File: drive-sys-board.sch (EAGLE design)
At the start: 31 parts, among them J2 APP_2POS_CONFIG12V_HORIZ, U1 OKI-78SR-5/1.5-W36HC, U2 MAX232D, U3 MAX232D, U4 MAX232D

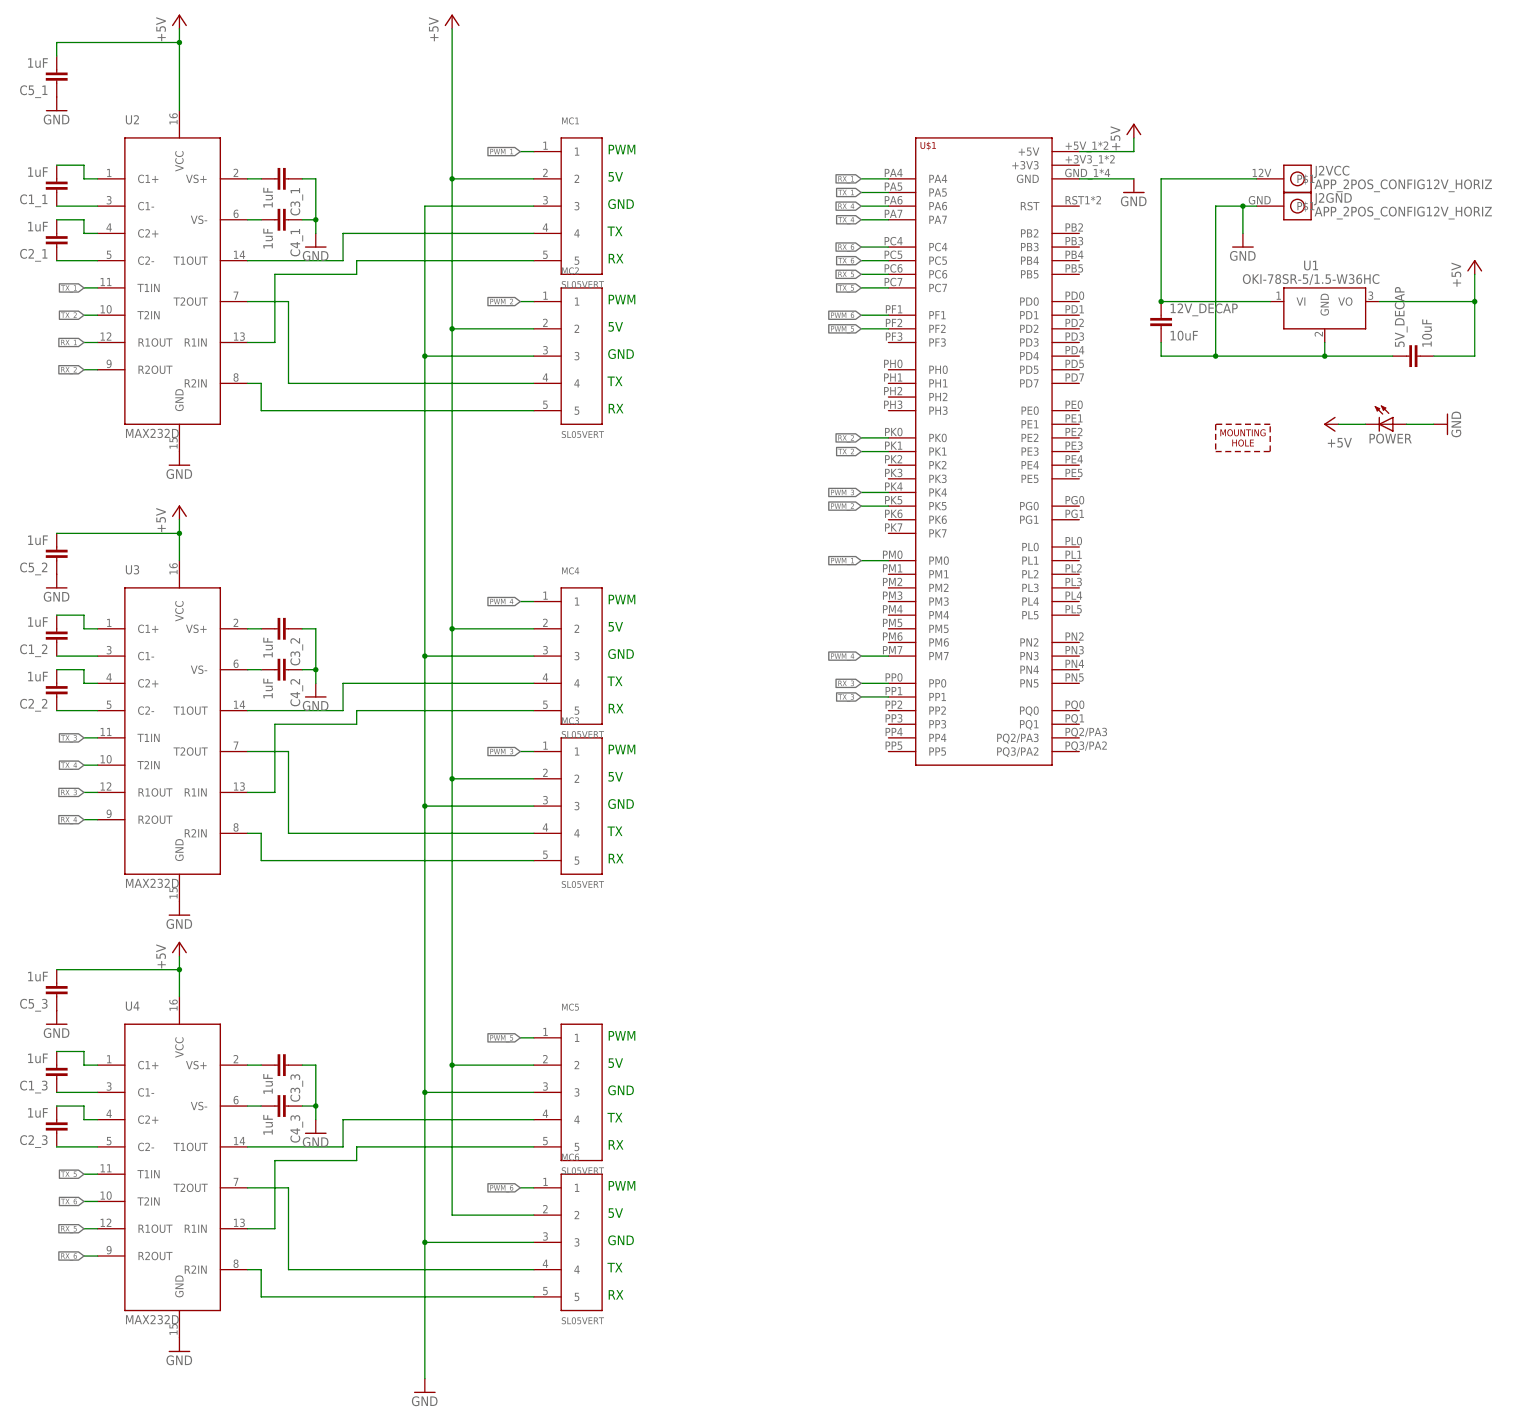
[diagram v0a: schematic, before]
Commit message: Prep for Board Review
- Labeled schematic with corresponding Serial channels (from hardware
serial on Tiva.
- Added Power Indicator LED and Debug LED
- Still need to decide on current limiting resistors for LEDs
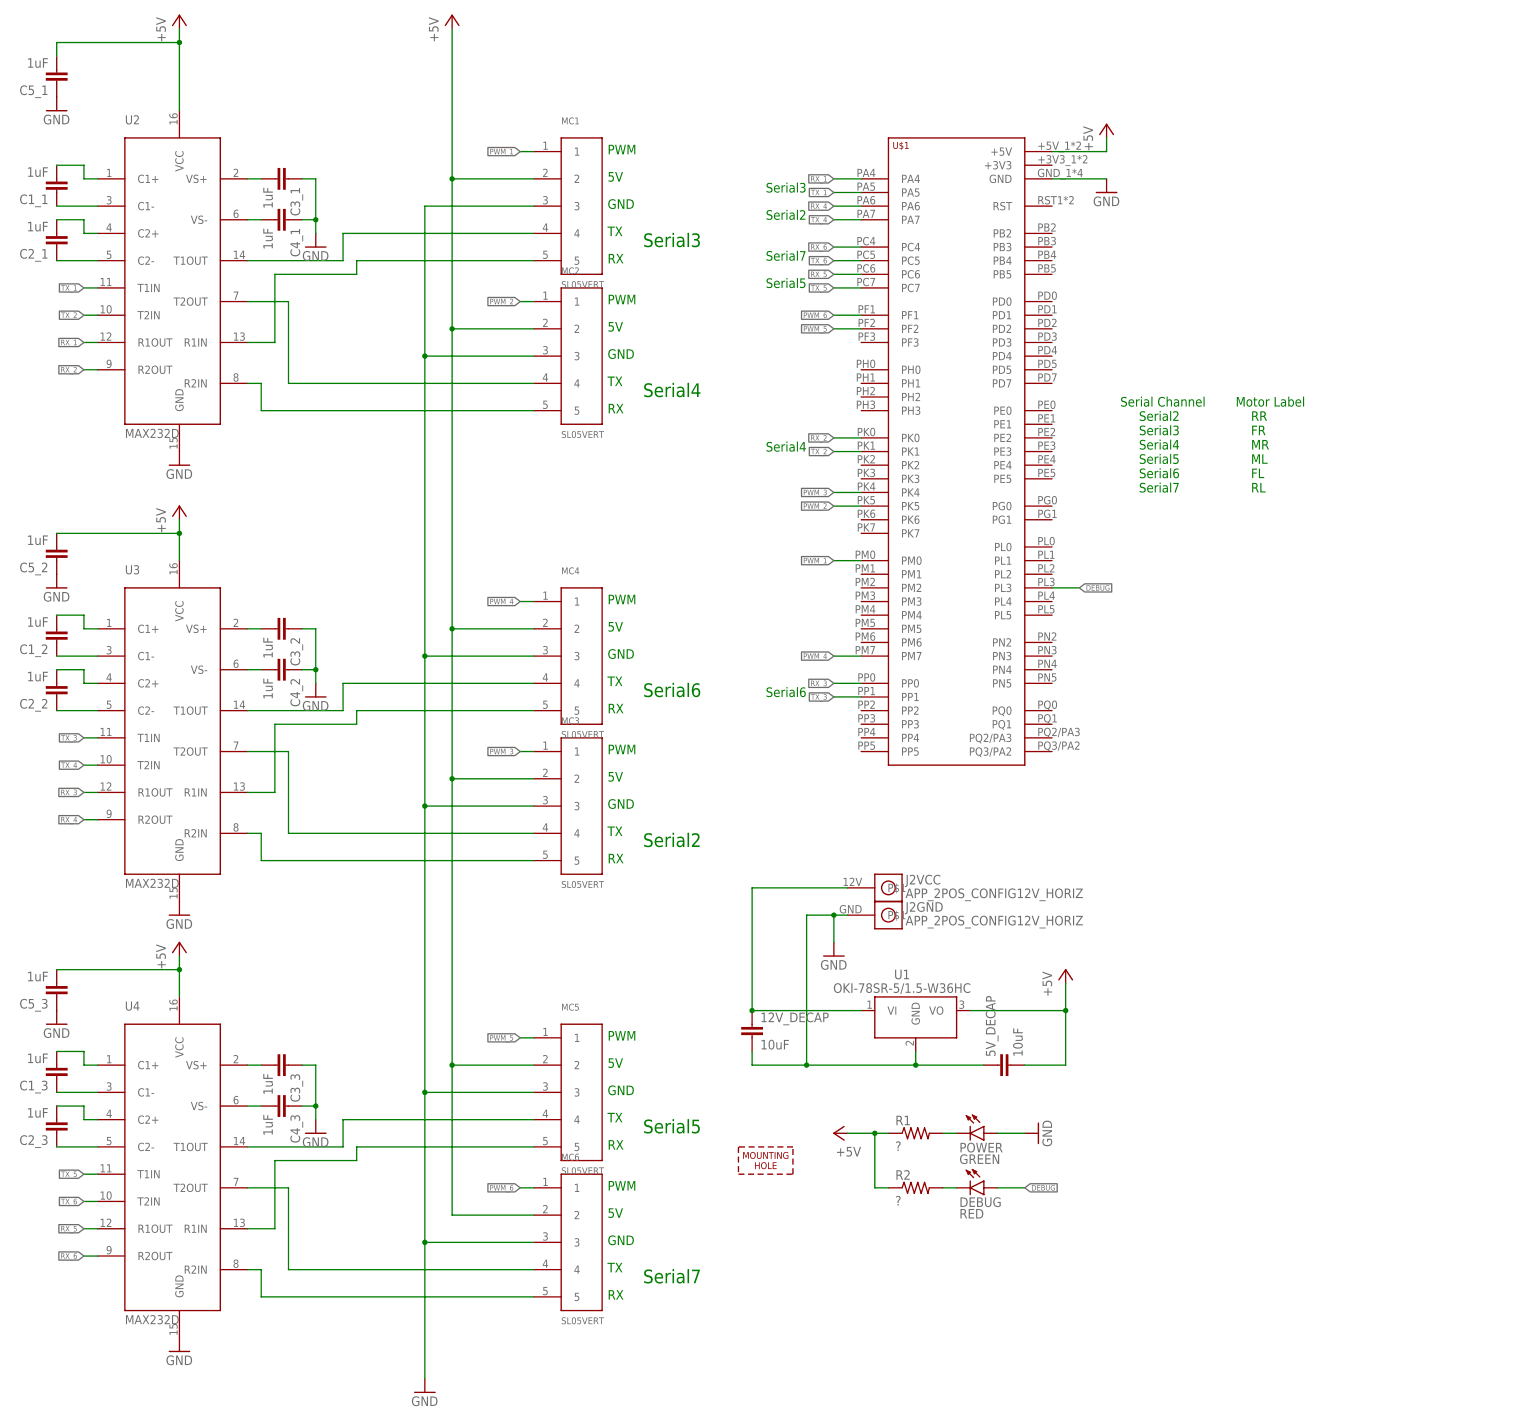
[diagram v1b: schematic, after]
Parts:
- added DEBUG: RED, SparkFun-LED:LED-RED1206
- added R1, R2: ?, SparkFun-Resistors:0.22OHM-1/4W-1%(0805)
- POWER: value (none) -> GREEN; device eagle-ltspice:LED_E -> SparkFun-LED:LED-GREEN1206
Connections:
- new net DEBUG: DEBUG.A, U$1.PL3
- new net N$10: DEBUG.C, R2.2
- new net N$17: POWER.C, R1.2
- net +5V: now also R1.1, R2.1; no longer POWER.C
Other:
- note added: "Serial Channel Motor Label Serial2 RR Serial3 FR Serial4 MR Serial5 ML Serial6 FL Serial7 RL"
- note added: "Serial2"
- note added: "Serial3"
- note added: "Serial4"
- note added: "Serial5"
- note added: "Serial6"
- note added: "Serial7"
- moved on the sheet: 12V_DECAP, 5V_DECAP, J2GND, J2VCC, U$1, U1

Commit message: Adjusted labels and removed top +5V plane
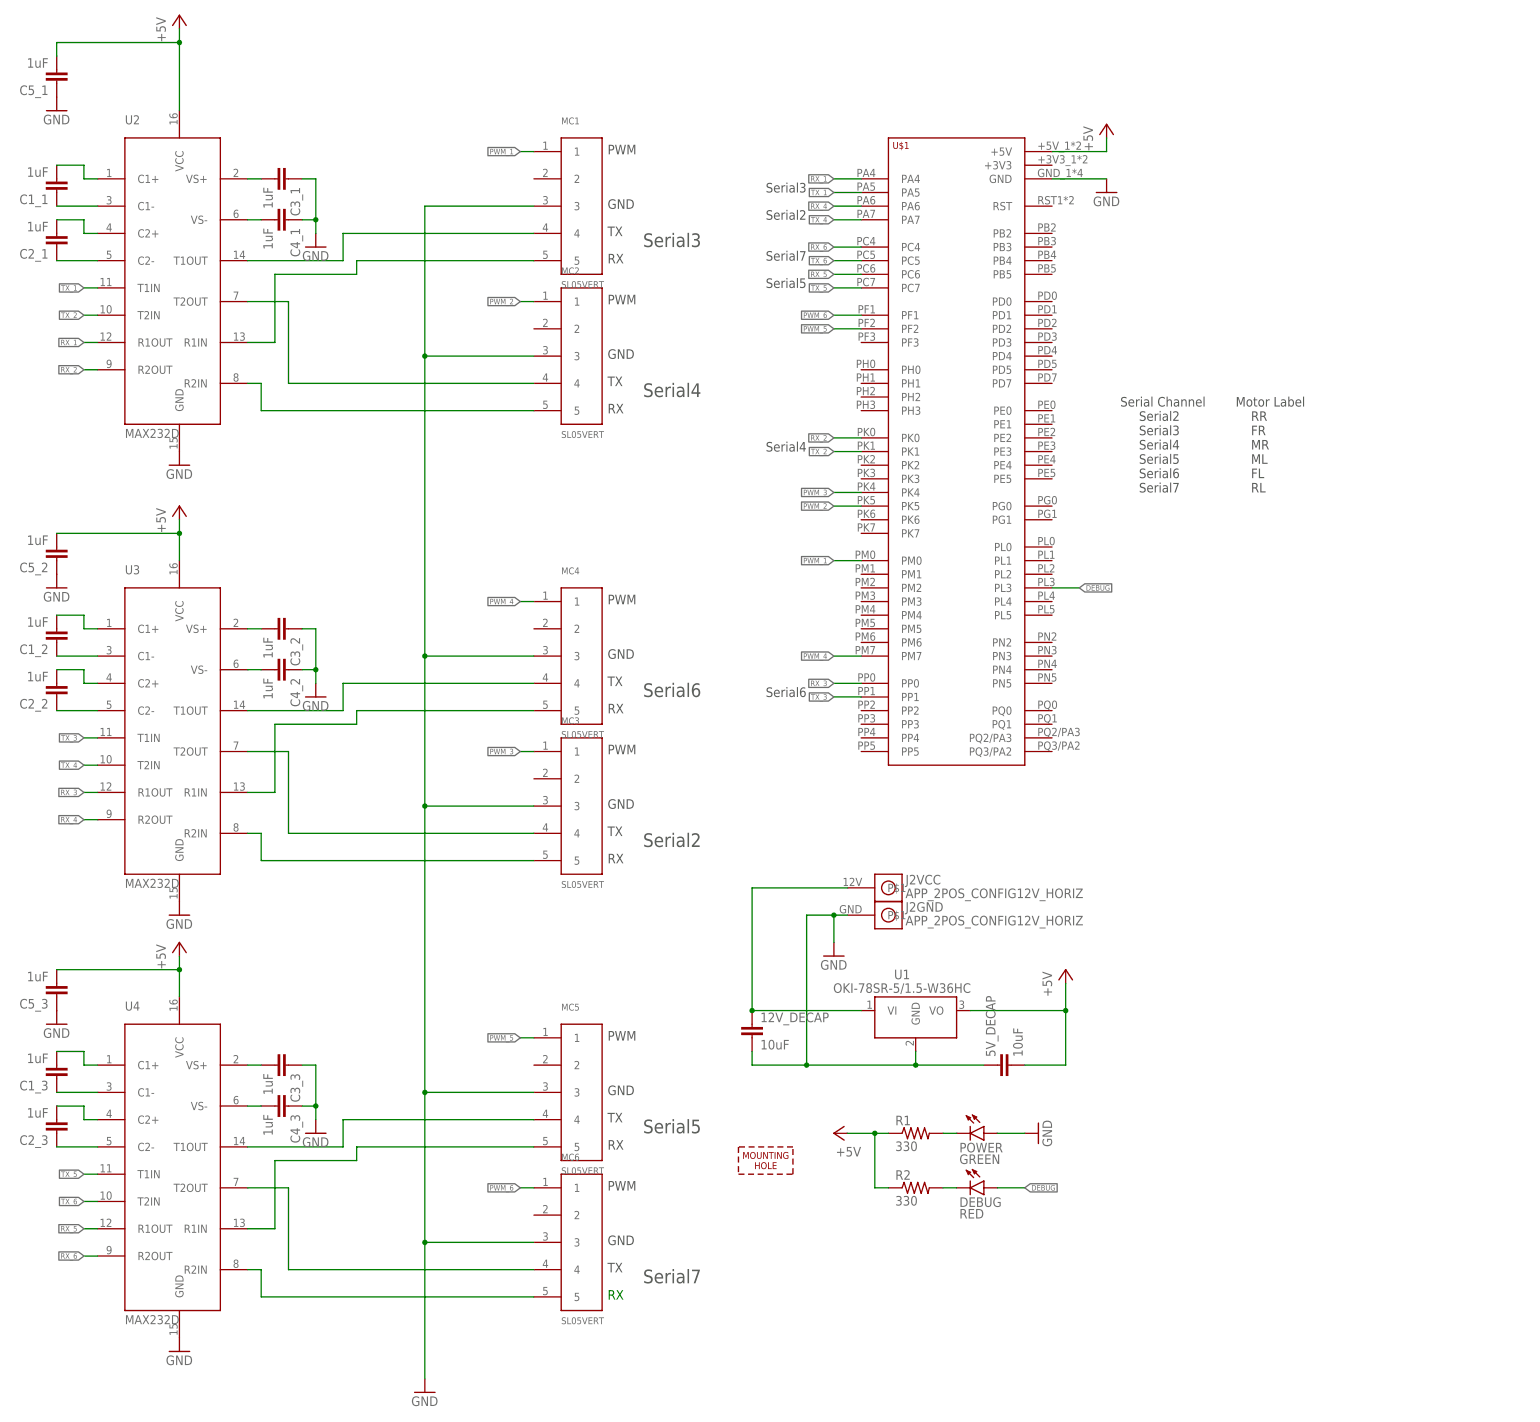
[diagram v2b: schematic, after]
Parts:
- R1, R2: value ? -> 330
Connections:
- net +5V: no longer MC1.2, MC2.2, MC3.2, MC4.2, MC5.2, MC6.2
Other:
- note removed: "5V"
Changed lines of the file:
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@@
 <part name="5V_DECAP" library="SparkFun-Capacitors" deviceset="CAP" device="0805" value="10uF"/>
 <part name="P+3" library="supply1" deviceset="+5V" device=""/>
-<part name="P+2" library="supply1" deviceset="+5V" device=""/>
 <part name="12V_DECAP" library="SparkFun-Capacitors" deviceset="CAP" device="0805" value="10uF"/>
 <part name="GND3" library="supply1" deviceset="GND" device=""/>
@@
 <part name="DEBUG" library="SparkFun-LED" deviceset="LED-RED" device="1206" value="RED"/>
 <part name="GND11" library="supply1" deviceset="GND" device=""/>
-<part name="R1" library="SparkFun-Resistors" deviceset="0.22OHM-1/4W-1%(0805)" device="" value="?"/>
-<part name="R2" library="SparkFun-Resistors" deviceset="0.22OHM-1/4W-1%(0805)" device="" value="?"/>
+<part name="R1" library="SparkFun-Resistors" deviceset="0.22OHM-1/4W-1%(0805)" device="" value="330"/>
+<part name="R2" library="SparkFun-Resistors" deviceset="0.22OHM-1/4W-1%(0805)" device="" value="330"/>
 </parts>
 <sheets>
 <sheet>
 <plain>
-<text x="-57.404" y="113.792" size="1.778" layer="91">PWM</text>
-<text x="-57.404" y="108.712" size="1.778" layer="91">5V</text>
-<text x="-57.404" y="103.632" size="1.778" layer="91">GND</text>
-<text x="-57.404" y="98.552" size="1.778" layer="91">TX</text>
-<text x="-57.404" y="93.472" size="1.778" layer="91">RX</text>
-<text x="-57.404" y="85.852" size="1.778" layer="91">PWM</text>
-<text x="-57.404" y="80.772" size="1.778" layer="91">5V</text>
-<text x="-57.404" y="75.692" size="1.778" layer="91">GND</text>
-<text x="-57.404" y="70.612" size="1.778" layer="91">TX</text>
-<text x="-57.404" y="65.532" size="1.778" layer="91">RX</text>
-<text x="-57.404" y="29.972" size="1.778" layer="91">PWM</text>
-<text x="-57.404" y="24.892" size="1.778" layer="91">5V</text>
-<text x="-57.404" y="19.812" size="1.778" layer="91">GND</text>
-<text x="-57.404" y="14.732" size="1.778" layer="91">TX</text>
-<text x="-57.404" y="9.652" size="1.778" layer="91">RX</text>
-<text x="-57.404" y="2.032" size="1.778" layer="91">PWM</text>
-<text x="-57.404" y="-3.048" size="1.778" layer="91">5V</text>
-<text x="-57.404" y="-8.128" size="1.778" layer="91">GND</text>
-<text x="-57.404" y="-13.208" size="1.778" layer="91">TX</text>
-<text x="-57.404" y="-18.288" size="1.778" layer="91">RX</text>
-<text x="-57.404" y="-51.308" size="1.778" layer="91">PWM</text>
-<text x="-57.404" y="-56.388" size="1.778" layer="91">5V</text>
-<text x="-57.404" y="-61.468" size="1.778" layer="91">GND</text>
-<text x="-57.404" y="-66.548" size="1.778" layer="91">TX</text>
-<text x="-57.404" y="-71.628" size="1.778" layer="91">RX</text>
-<text x="-57.404" y="-79.248" size="1.778" layer="91">PWM</text>
-<text x="-57.404" y="-84.328" size="1.778" layer="91">5V</text>
-<text x="-57.404" y="-89.408" size="1.778" layer="91">GND</text>
-<text x="-57.404" y="-94.488" size="1.778" layer="91">TX</text>
+<text x="-57.404" y="113.792" size="1.778" layer="97">PWM</text>
+<text x="-57.404" y="103.632" size="1.778" layer="97">GND</text>
+<text x="-57.404" y="98.552" size="1.778" layer="97">TX</text>
+<text x="-57.404" y="93.472" size="1.778" layer="97">RX</text>
+<text x="-57.404" y="85.852" size="1.778" layer="97">PWM</text>
+<text x="-57.404" y="75.692" size="1.778" layer="97">GND</text>
+<text x="-57.404" y="70.612" size="1.778" layer="97">TX</text>
+<text x="-57.404" y="65.532" size="1.778" layer="97">RX</text>
+<text x="-57.404" y="29.972" size="1.778" layer="97">PWM</text>
+<text x="-57.404" y="19.812" size="1.778" layer="97">GND</text>
+<text x="-57.404" y="14.732" size="1.778" layer="97">TX</text>
+<text x="-57.404" y="9.652" size="1.778" layer="97">RX</text>
+<text x="-57.404" y="2.032" size="1.778" layer="97">PWM</text>
+<text x="-57.404" y="-8.128" size="1.778" layer="97">GND</text>
+<text x="-57.404" y="-13.208" size="1.778" layer="97">TX</text>
+<text x="-57.404" y="-18.288" size="1.778" layer="97">RX</text>
+<text x="-57.404" y="-51.308" size="1.778" layer="97">PWM</text>
+<text x="-57.404" y="-61.468" size="1.778" layer="97">GND</text>
+<text x="-57.404" y="-66.548" size="1.778" layer="97">TX</text>
+<text x="-57.404" y="-71.628" size="1.778" layer="97">RX</text>
+<text x="-57.404" y="-79.248" size="1.778" layer="97">PWM</text>
+<text x="-57.404" y="-89.408" size="1.778" layer="97">GND</text>
+<text x="-57.404" y="-94.488" size="1.778" layer="97">TX</text>
 <text x="-57.404" y="-99.568" size="1.778" layer="91">RX</text>
-<text x="-27.94" y="101.6" size="1.778" layer="91">Serial2</text>
-<text x="-27.94" y="106.68" size="1.778" layer="91">Serial3</text>
-<text x="-27.94" y="93.98" size="1.778" layer="91">Serial7</text>
-<text x="-27.94" y="88.9" size="1.778" layer="91">Serial5</text>
-<text x="-27.94" y="58.42" size="1.778" layer="91">Serial4</text>
-<text x="-27.94" y="12.7" size="1.778" layer="91">Serial6</text>
-<text x="-50.8" y="96.52" size="2.54" layer="91">Serial3</text>
-<text x="-50.8" y="-15.24" size="2.54" layer="91">Serial2</text>
-<text x="-50.8" y="-96.52" size="2.54" layer="91">Serial7</text>
-<text x="-50.8" y="-68.58" size="2.54" layer="91">Serial5</text>
-<text x="-50.8" y="68.58" size="2.54" layer="91">Serial4</text>
-<text x="-50.8" y="12.7" size="2.54" layer="91">Serial6</text>
-<text x="38.1" y="50.8" size="1.778" layer="91">Serial Channel        Motor Label
+<text x="-27.94" y="101.6" size="1.778" layer="97">Serial2</text>
+<text x="-27.94" y="106.68" size="1.778" layer="97">Serial3</text>
+<text x="-27.94" y="93.98" size="1.778" layer="97">Serial7</text>
+<text x="-27.94" y="88.9" size="1.778" layer="97">Serial5</text>
+<text x="-27.94" y="58.42" size="1.778" layer="97">Serial4</text>
+<text x="-27.94" y="12.7" size="1.778" layer="97">Serial6</text>
+<text x="-50.8" y="96.52" size="2.54" layer="97">Serial3</text>
+<text x="-50.8" y="-15.24" size="2.54" layer="97">Serial2</text>
+<text x="-50.8" y="-96.52" size="2.54" layer="97">Serial7</text>
+<text x="-50.8" y="-68.58" size="2.54" layer="97">Serial5</text>
+<text x="-50.8" y="68.58" size="2.54" layer="97">Serial4</text>
+<text x="-50.8" y="12.7" size="2.54" layer="97">Serial6</text>
+<text x="38.1" y="50.8" size="1.778" layer="97">Serial Channel        Motor Label
      Serial2                   RR
      Serial3                   FR
@@
 <instance part="5V_DECAP" gate="G$1" x="17.78" y="-55.88" rot="R90"/>
 <instance part="P+3" gate="1" x="-137.16" y="139.7"/>
-<instance part="P+2" gate="1" x="-86.36" y="139.7"/>
 <instance part="12V_DECAP" gate="G$1" x="-30.48" y="-50.8"/>
 <instance part="GND3" gate="1" x="-137.16" y="-27.94"/>
@@
 </segment>
 <segment>
-<wire x1="-86.36" y1="137.16" x2="-86.36" y2="109.22" width="0.1524" layer="91"/>
-<pinref part="MC6" gate="G$1" pin="2"/>
-<wire x1="-86.36" y1="109.22" x2="-86.36" y2="81.28" width="0.1524" layer="91"/>
-<wire x1="-86.36" y1="81.28" x2="-86.36" y2="25.4" width="0.1524" layer="91"/>
-<wire x1="-86.36" y1="25.4" x2="-86.36" y2="-2.54" width="0.1524" layer="91"/>
-<wire x1="-86.36" y1="-2.54" x2="-86.36" y2="-55.88" width="0.1524" layer="91"/>
-<wire x1="-86.36" y1="-55.88" x2="-86.36" y2="-83.82" width="0.1524" layer="91"/>
-<wire x1="-86.36" y1="-83.82" x2="-71.12" y2="-83.82" width="0.1524" layer="91"/>
-<pinref part="MC5" gate="G$1" pin="2"/>
-<wire x1="-71.12" y1="-55.88" x2="-86.36" y2="-55.88" width="0.1524" layer="91"/>
-<junction x="-86.36" y="-55.88"/>
-<pinref part="MC3" gate="G$1" pin="2"/>
-<wire x1="-71.12" y1="-2.54" x2="-86.36" y2="-2.54" width="0.1524" layer="91"/>
-<junction x="-86.36" y="-2.54"/>
-<pinref part="MC4" gate="G$1" pin="2"/>
-<wire x1="-71.12" y1="25.4" x2="-86.36" y2="25.4" width="0.1524" layer="91"/>
-<junction x="-86.36" y="25.4"/>
-<pinref part="MC2" gate="G$1" pin="2"/>
-<wire x1="-71.12" y1="81.28" x2="-86.36" y2="81.28" width="0.1524" layer="91"/>
-<junction x="-86.36" y="81.28"/>
-<pinref part="MC1" gate="G$1" pin="2"/>
-<wire x1="-71.12" y1="109.22" x2="-86.36" y2="109.22" width="0.1524" layer="91"/>
-<junction x="-86.36" y="109.22"/>
-<pinref part="P+2" gate="1" pin="+5V"/>
-</segment>
-<segment>
